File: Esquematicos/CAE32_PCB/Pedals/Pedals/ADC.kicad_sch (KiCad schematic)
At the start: 16 parts, among them J10 Conn_01x03_Female, J11 Conn_01x03_Female, J12 Conn_01x03_Female, J13 Conn_01x03_Female, J3 Conn_01x03_Female, J4 Conn_01x03_Female, J5 Conn_01x03_Female, J6 Conn_01x03_Female, J7 Conn_01x03_Female, J8 Conn_01x03_Female, J9 Conn_01x03_Female, U2 REF3033, U3 ADC128S102

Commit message: update: Componentes acomodados en la PCB
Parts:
- renumbered J9 to J10, J10 to J11, J11 to J12, J12 to J13, J13 to J14, J3 to J4, J4 to J5, J5 to J6, J6 to J7, J7 to J8, J8 to J9
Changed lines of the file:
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@@
   (symbol (lib_id "Connector:Conn_01x03_Female") (at 269.875 40.005 0) (unit 1)
     (in_bom yes) (on_board yes)
-    (property "Reference" "J11" (id 0) (at 268.605 34.925 0)
+    (property "Reference" "J12" (id 0) (at 268.605 34.925 0)
       (effects (font (size 1.27 1.27)) (justify left))
     )
@@
   (symbol (lib_id "Connector:Conn_01x03_Female") (at 250.19 92.71 0) (unit 1)
     (in_bom yes) (on_board yes)
-    (property "Reference" "J9" (id 0) (at 248.92 87.63 0)
+    (property "Reference" "J10" (id 0) (at 248.92 87.63 0)
       (effects (font (size 1.27 1.27)) (justify left))
     )
@@
   (symbol (lib_id "Connector:Conn_01x03_Female") (at 231.14 68.58 0) (unit 1)
     (in_bom yes) (on_board yes)
-    (property "Reference" "J4" (id 0) (at 229.87 63.5 0)
+    (property "Reference" "J5" (id 0) (at 229.87 63.5 0)
       (effects (font (size 1.27 1.27)) (justify left))
     )
@@
   (symbol (lib_id "Connector:Conn_01x03_Female") (at 249.555 40.005 0) (unit 1)
     (in_bom yes) (on_board yes)
-    (property "Reference" "J7" (id 0) (at 248.285 34.925 0)
+    (property "Reference" "J8" (id 0) (at 248.285 34.925 0)
       (effects (font (size 1.27 1.27)) (justify left))
     )
@@
   (symbol (lib_id "Connector:Conn_01x03_Female") (at 270.51 68.58 0) (unit 1)
     (in_bom yes) (on_board yes)
-    (property "Reference" "J12" (id 0) (at 269.24 63.5 0)
+    (property "Reference" "J13" (id 0) (at 269.24 63.5 0)
       (effects (font (size 1.27 1.27)) (justify left))
     )
@@
   (symbol (lib_id "Connector:Conn_01x03_Female") (at 250.825 118.11 0) (unit 1)
     (in_bom yes) (on_board yes)
-    (property "Reference" "J10" (id 0) (at 249.555 113.03 0)
+    (property "Reference" "J11" (id 0) (at 249.555 113.03 0)
       (effects (font (size 1.27 1.27)) (justify left))
     )
@@
   (symbol (lib_id "Connector:Conn_01x03_Female") (at 250.19 68.58 0) (unit 1)
     (in_bom yes) (on_board yes)
-    (property "Reference" "J8" (id 0) (at 248.92 63.5 0)
+    (property "Reference" "J9" (id 0) (at 248.92 63.5 0)
       (effects (font (size 1.27 1.27)) (justify left))
     )
@@
   (symbol (lib_id "Connector:Conn_01x03_Female") (at 270.51 92.71 0) (unit 1)
     (in_bom yes) (on_board yes)
-    (property "Reference" "J13" (id 0) (at 269.24 87.63 0)
+    (property "Reference" "J14" (id 0) (at 269.24 87.63 0)
       (effects (font (size 1.27 1.27)) (justify left))
     )
@@
   (symbol (lib_id "Connector:Conn_01x03_Female") (at 230.505 40.005 0) (unit 1)
     (in_bom yes) (on_board yes)
-    (property "Reference" "J3" (id 0) (at 229.235 34.925 0)
+    (property "Reference" "J4" (id 0) (at 229.235 34.925 0)
       (effects (font (size 1.27 1.27)) (justify left))
     )
@@
   (symbol (lib_id "Connector:Conn_01x03_Female") (at 231.775 118.11 0) (unit 1)
     (in_bom yes) (on_board yes)
-    (property "Reference" "J6" (id 0) (at 230.505 113.03 0)
+    (property "Reference" "J7" (id 0) (at 230.505 113.03 0)
       (effects (font (size 1.27 1.27)) (justify left))
     )
@@
   (symbol (lib_id "Connector:Conn_01x03_Female") (at 231.14 92.71 0) (unit 1)
     (in_bom yes) (on_board yes)
-    (property "Reference" "J5" (id 0) (at 229.87 87.63 0)
-      (effects (font (size 1.27 1.27)) (justify left))
-    )
+    (property "Reference" "J6" (id 0) (at 229.87 87.63 0)
+      (effects (font (size 1.27 1.27)) (justify left))
+    )

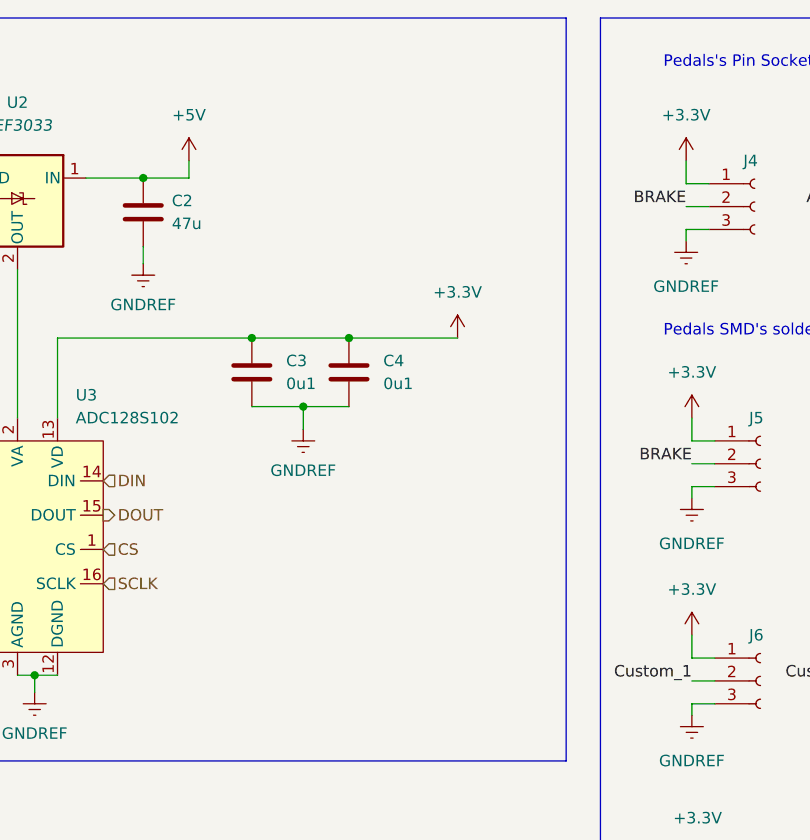
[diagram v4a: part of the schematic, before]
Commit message: update: se agrega el consumo de corriente a los IC's ademas de agregar el URL y numero de parte de los componentes de LCSC en kicad
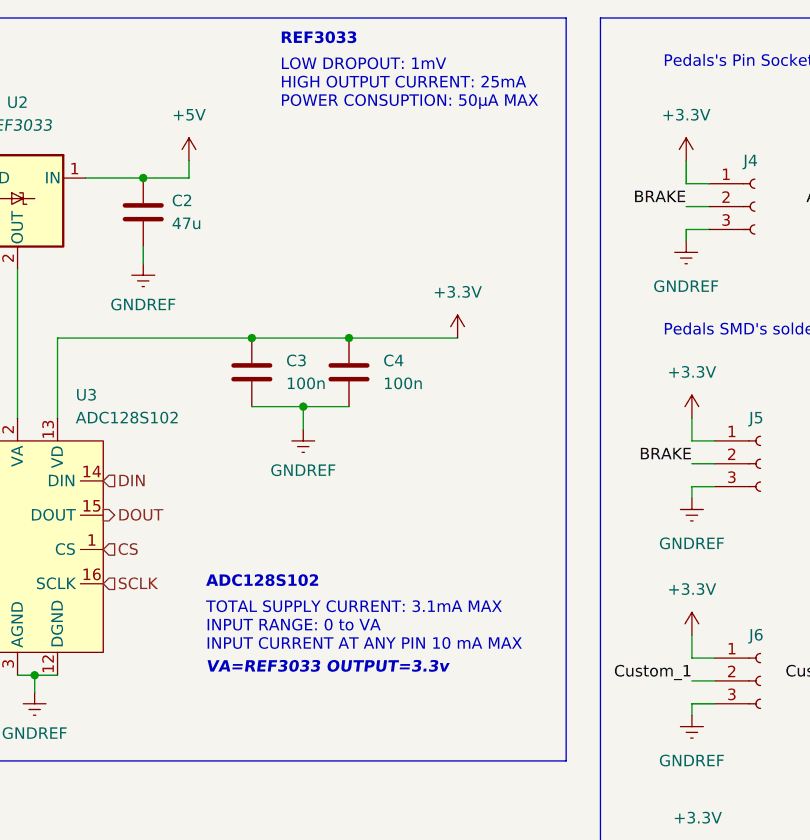
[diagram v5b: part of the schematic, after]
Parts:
- C2: LCSC_PART (none) -> C140782
- C3, C4: value 0u1 -> 100n; LCSC_PART (none) -> c1591
- J12, J4, J8: LCSC_PART (none) -> C146243
- U2: LCSC_PART (none) -> C36658
- U3: LCSC_PART (none) -> C179666
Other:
- note added: "ADC128S102"
- note added: "LOW DROPOUT: 1mV HIGH OUTPUT CURRENT: 25mA POWER CONSUPTION: 50μA MAX"
- note added: "REF3033"
- note added: "TOTAL SUPPLY CURRENT: 3.1mA MAX INPUT RANGE: 0 to VA INPUT CURRENT AT ANY PIN 10 mA MAX"
- note added: "VA=REF3033 OUTPUT=3.3v"
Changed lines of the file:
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@@
     (stroke (width 0) (type default) (color 0 0 0 0))
+  )
+  (text "LOW DROPOUT: 1mV\nHIGH OUTPUT CURRENT: 25mA\nPOWER CONSUPTION: 50μA MAX "
+    (at 177.8 29.21 0)
+    (effects (font (size 1.27 1.27)) (justify left bottom))
   )
   (text "ADC Multiplexer" (at 128.27 22.86 0)
     (effects (font (size 1.27 1.27)) (justify left bottom))
   )
+  (text "VA=REF3033 OUTPUT=3.3v" (at 169.545 92.075 0)
+    (effects (font (size 1.27 1.27) (thickness 0.254) bold italic) (justify left bottom))
+  )
+  (text "ADC128S102" (at 169.545 82.55 0)
+    (effects (font (size 1.27 1.27) (thickness 0.254) bold) (justify left bottom))
+  )
   (text "Pedals's Pin Socket" (at 220.345 24.765 0)
     (effects (font (size 1.27 1.27)) (justify left bottom))
   )
+  (text "REF3033" (at 177.8 22.225 0)
+    (effects (font (size 1.27 1.27) (thickness 0.254) bold) (justify left bottom))
+  )
   (text "Pedals SMD's solder point" (at 220.345 54.61 0)
     (effects (font (size 1.27 1.27)) (justify left bottom))
   )
+  (text "TOTAL SUPPLY CURRENT: 3.1mA MAX\nINPUT RANGE: 0 to VA\nINPUT CURRENT AT ANY PIN 10 mA MAX\n"
+    (at 169.545 89.535 0)
+    (effects (font (size 1.27 1.27)) (justify left bottom))
+  )
   (label "CLUTCH" (at 262.255 40.005 180)
     (effects (font (size 1.27 1.27)) (justify right bottom))
@@
       (effects (font (size 1.27 1.27)) hide)
     )
+    (property "LCSC_PART" "C146243" (id 4) (at 269.875 40.005 0)
+      (effects (font (size 1.27 1.27)) hide)
+    )
     (pin "1")
     (pin "2")
@@
       (effects (font (size 1.27 1.27)) hide)
     )
+    (property "LCSC_PART" "C146243" (id 4) (at 249.555 40.005 0)
+      (effects (font (size 1.27 1.27)) hide)
+    )
     (pin "1")
     (pin "2")
@@
       (effects (font (size 1.27 1.27)) (justify left))
     )
-    (property "Value" "0u1" (id 1) (at 178.435 59.6899 0)
+    (property "Value" "100n" (id 1) (at 178.435 59.6899 0)
       (effects (font (size 1.27 1.27)) (justify left))
     )
@@
     )
     (property "Datasheet" "~" (id 3) (at 174.625 58.42 0)
+      (effects (font (size 1.27 1.27)) hide)
+    )
+    (property "LCSC_PART" "c1591" (id 4) (at 174.625 58.42 0)
       (effects (font (size 1.27 1.27)) hide)
     )
@@
       (effects (font (size 1.27 1.27)) hide)
     )
+    (property "LCSC_PART" "C140782" (id 4) (at 162.56 40.64 0)
+      (effects (font (size 1.27 1.27)) hide)
+    )
     (pin "1")
     (pin "2")
@@
       (effects (font (size 1.27 1.27)) (justify left))
     )
-    (property "Value" "0u1" (id 1) (at 189.23 59.6899 0)
+    (property "Value" "100n" (id 1) (at 189.23 59.6899 0)
       (effects (font (size 1.27 1.27)) (justify left))
     )
@@
     )
     (property "Datasheet" "~" (id 3) (at 185.42 58.42 0)
+      (effects (font (size 1.27 1.27)) hide)
+    )
+    (property "LCSC_PART" "c1591" (id 4) (at 185.42 58.42 0)
       (effects (font (size 1.27 1.27)) hide)
     )
@@
       (effects (font (size 1.27 1.27) italic) hide)
     )
+    (property "LCSC_PART" "C36658" (id 4) (at 148.59 39.37 0)
+      (effects (font (size 1.27 1.27)) hide)
+    )
     (pin "1")
     (pin "2")
@@
       (effects (font (size 1.27 1.27)) hide)
     )
-    (property "Datasheet" "" (id 3) (at 150.495 71.755 0)
+    (property "Datasheet" "https://datasheet.lcsc.com/lcsc/2304140030_Texas-Instruments-ADC128S102CIMTX-NOPB_C179666.pdf" (id 3) (at 150.495 71.755 0)
+      (effects (font (size 1.27 1.27)) hide)
+    )
+    (property "LCSC_PART" "C179666" (id 4) (at 150.495 76.835 0)
       (effects (font (size 1.27 1.27)) hide)
     )
@@
       (effects (font (size 1.27 1.27)) hide)
     )
+    (property "LCSC_PART" "C146243" (id 4) (at 230.505 40.005 0)
+      (effects (font (size 1.27 1.27)) hide)
+    )

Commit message: update: se crea la primera revisión de la PCB
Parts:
- C2: Item (none) -> C140782; Qty (none) -> 1; Vendor (none) -> C140782
- C3, C4: Item (none) -> c1591; Qty (none) -> 22; Vendor (none) -> c1591
- J10, J11, J13, J14, J5, J6, J7, J9: Qty (none) -> 8
- J12, J4, J8: Item (none) -> C146243; Qty (none) -> 3; Vendor (none) -> C146243
- U2: Item (none) -> C36658; Qty (none) -> 1; Vendor (none) -> C36658
- U3: Item (none) -> C179666; Qty (none) -> 1; Vendor (none) -> C179666
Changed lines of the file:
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@@
+      (effects (font (size 1.27 1.27)) hide)
+    )
+    (property "Item" "C146243" (id 5) (at 269.875 40.005 0)
+      (effects (font (size 1.27 1.27)) hide)
+    )
+    (property "Qty" "3" (id 6) (at 269.875 40.005 0)
+      (effects (font (size 1.27 1.27)) hide)
+    )
+    (property "Vendor" "C146243" (id 7) (at 269.875 40.005 0)
       (effects (font (size 1.27 1.27)) hide)
     )
@@
       (effects (font (size 1.27 1.27)) hide)
     )
+    (property "Qty" "8" (id 4) (at 250.19 92.71 0)
+      (effects (font (size 1.27 1.27)) hide)
+    )
     (pin "1")
     (pin "2")
@@
     )
     (property "Datasheet" "~" (id 3) (at 231.14 68.58 0)
+      (effects (font (size 1.27 1.27)) hide)
+    )
+    (property "Qty" "8" (id 4) (at 231.14 68.58 0)
       (effects (font (size 1.27 1.27)) hide)
     )
@@
       (effects (font (size 1.27 1.27)) hide)
     )
+    (property "Item" "C146243" (id 5) (at 249.555 40.005 0)
+      (effects (font (size 1.27 1.27)) hide)
+    )
+    (property "Qty" "3" (id 6) (at 249.555 40.005 0)
+      (effects (font (size 1.27 1.27)) hide)
+    )
+    (property "Vendor" "C146243" (id 7) (at 249.555 40.005 0)
+      (effects (font (size 1.27 1.27)) hide)
+    )
     (pin "1")
     (pin "2")
@@
       (effects (font (size 1.27 1.27)) hide)
     )
+    (property "Item" "c1591" (id 5) (at 174.625 58.42 0)
+      (effects (font (size 1.27 1.27)) hide)
+    )
+    (property "Qty" "22" (id 6) (at 174.625 58.42 0)
+      (effects (font (size 1.27 1.27)) hide)
+    )
+    (property "Vendor" "c1591" (id 7) (at 174.625 58.42 0)
+      (effects (font (size 1.27 1.27)) hide)
+    )
     (pin "1")
     (pin "2")
@@
       (effects (font (size 1.27 1.27)) hide)
     )
+    (property "Item" "C140782" (id 5) (at 162.56 40.64 0)
+      (effects (font (size 1.27 1.27)) hide)
+    )
+    (property "Qty" "1" (id 6) (at 162.56 40.64 0)
+      (effects (font (size 1.27 1.27)) hide)
+    )
+    (property "Vendor" "C140782" (id 7) (at 162.56 40.64 0)
+      (effects (font (size 1.27 1.27)) hide)
+    )
     (pin "1")
     (pin "2")
@@
     )
     (property "LCSC_PART" "c1591" (id 4) (at 185.42 58.42 0)
+      (effects (font (size 1.27 1.27)) hide)
+    )
+    (property "Item" "c1591" (id 5) (at 185.42 58.42 0)
+      (effects (font (size 1.27 1.27)) hide)
+    )
+    (property "Qty" "22" (id 6) (at 185.42 58.42 0)
+      (effects (font (size 1.27 1.27)) hide)
+    )
+    (property "Vendor" "c1591" (id 7) (at 185.42 58.42 0)
       (effects (font (size 1.27 1.27)) hide)
     )
@@
       (effects (font (size 1.27 1.27)) hide)
     )
+    (property "Qty" "8" (id 4) (at 270.51 68.58 0)
+      (effects (font (size 1.27 1.27)) hide)
+    )
     (pin "1")
     (pin "2")
@@
       (effects (font (size 1.27 1.27)) hide)
     )
+    (property "Qty" "8" (id 4) (at 250.825 118.11 0)
+      (effects (font (size 1.27 1.27)) hide)
+    )
     (pin "1")
     (pin "2")
@@
     )
     (property "Datasheet" "~" (id 3) (at 250.19 68.58 0)
+      (effects (font (size 1.27 1.27)) hide)
+    )
+    (property "Qty" "8" (id 4) (at 250.19 68.58 0)
       (effects (font (size 1.27 1.27)) hide)
     )
@@
       (effects (font (size 1.27 1.27)) hide)
     )
+    (property "Item" "C36658" (id 5) (at 148.59 39.37 0)
+      (effects (font (size 1.27 1.27)) hide)
+    )
+    (property "Qty" "1" (id 6) (at 148.59 39.37 0)
+      (effects (font (size 1.27 1.27)) hide)
+    )
+    (property "Vendor" "C36658" (id 7) (at 148.59 39.37 0)
+      (effects (font (size 1.27 1.27)) hide)
+    )
     (pin "1")
     (pin "2")
@@
     )
     (property "LCSC_PART" "C179666" (id 4) (at 150.495 76.835 0)
+      (effects (font (size 1.27 1.27)) hide)
+    )
+    (property "Item" "C179666" (id 5) (at 150.495 76.835 0)
+      (effects (font (size 1.27 1.27)) hide)
+    )
+    (property "Qty" "1" (id 6) (at 150.495 76.835 0)
+      (effects (font (size 1.27 1.27)) hide)
+    )
+    (property "Vendor" "C179666" (id 7) (at 150.495 76.835 0)
       (effects (font (size 1.27 1.27)) hide)
     )
@@
       (effects (font (size 1.27 1.27)) hide)
     )
+    (property "Qty" "8" (id 4) (at 270.51 92.71 0)
+      (effects (font (size 1.27 1.27)) hide)
+    )
     (pin "1")
     (pin "2")
@@
       (effects (font (size 1.27 1.27)) hide)
     )
+    (property "Item" "C146243" (id 5) (at 230.505 40.005 0)
+      (effects (font (size 1.27 1.27)) hide)
+    )
+    (property "Qty" "3" (id 6) (at 230.505 40.005 0)
+      (effects (font (size 1.27 1.27)) hide)
+    )
+    (property "Vendor" "C146243" (id 7) (at 230.505 40.005 0)
+      (effects (font (size 1.27 1.27)) hide)
+    )
     (pin "1")
     (pin "2")
@@
       (effects (font (size 1.27 1.27)) hide)
     )
+    (property "Qty" "8" (id 4) (at 231.775 118.11 0)
+      (effects (font (size 1.27 1.27)) hide)
+    )
     (pin "1")
     (pin "2")
@@
       (effects (font (size 1.27 1.27)) hide)
     )
+    (property "Qty" "8" (id 4) (at 231.14 92.71 0)
+      (effects (font (size 1.27 1.27)) hide)
+    )

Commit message: chore: arrange schematics components
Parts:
- C2, C3, C4: footprint Capacitor_SMD:C_0603_1608Metric_Pad1.08x0.95mm_HandSolder -> Capacitor_SMD:C_0603_1608Metric

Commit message: update: added minor improvements to Pedal's PCB
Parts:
- U3: value ADC128S102 -> ADC128S022; LCSC_PART C179666 -> C180424; Vendor C179666 -> C180424
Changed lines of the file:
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@@
       (effects (font (size 1.27 1.27)) (justify left))
     )
-    (property "Value" "ADC128S102" (at 155.0544 63.5 0)
+    (property "Value" "ADC128S022" (at 155.0544 63.5 0)
       (effects (font (size 1.27 1.27)) (justify left))
     )
@@
       (effects (font (size 1.27 1.27)) hide)
     )
-    (property "LCSC_PART" "C179666" (at 150.495 76.835 0)
+    (property "LCSC_PART" "C180424" (at 150.495 76.835 0)
       (effects (font (size 1.27 1.27)) hide)
     )
@@
       (effects (font (size 1.27 1.27)) hide)
     )
-    (property "Vendor" "C179666" (at 150.495 76.835 0)
+    (property "Vendor" "C180424" (at 150.495 76.835 0)
       (effects (font (size 1.27 1.27)) hide)
     )
